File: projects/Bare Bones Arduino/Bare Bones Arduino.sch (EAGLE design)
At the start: 14 parts, among them IC1 AVR-MEGA8-P, J1 POWER_JACKPTH_LOCK

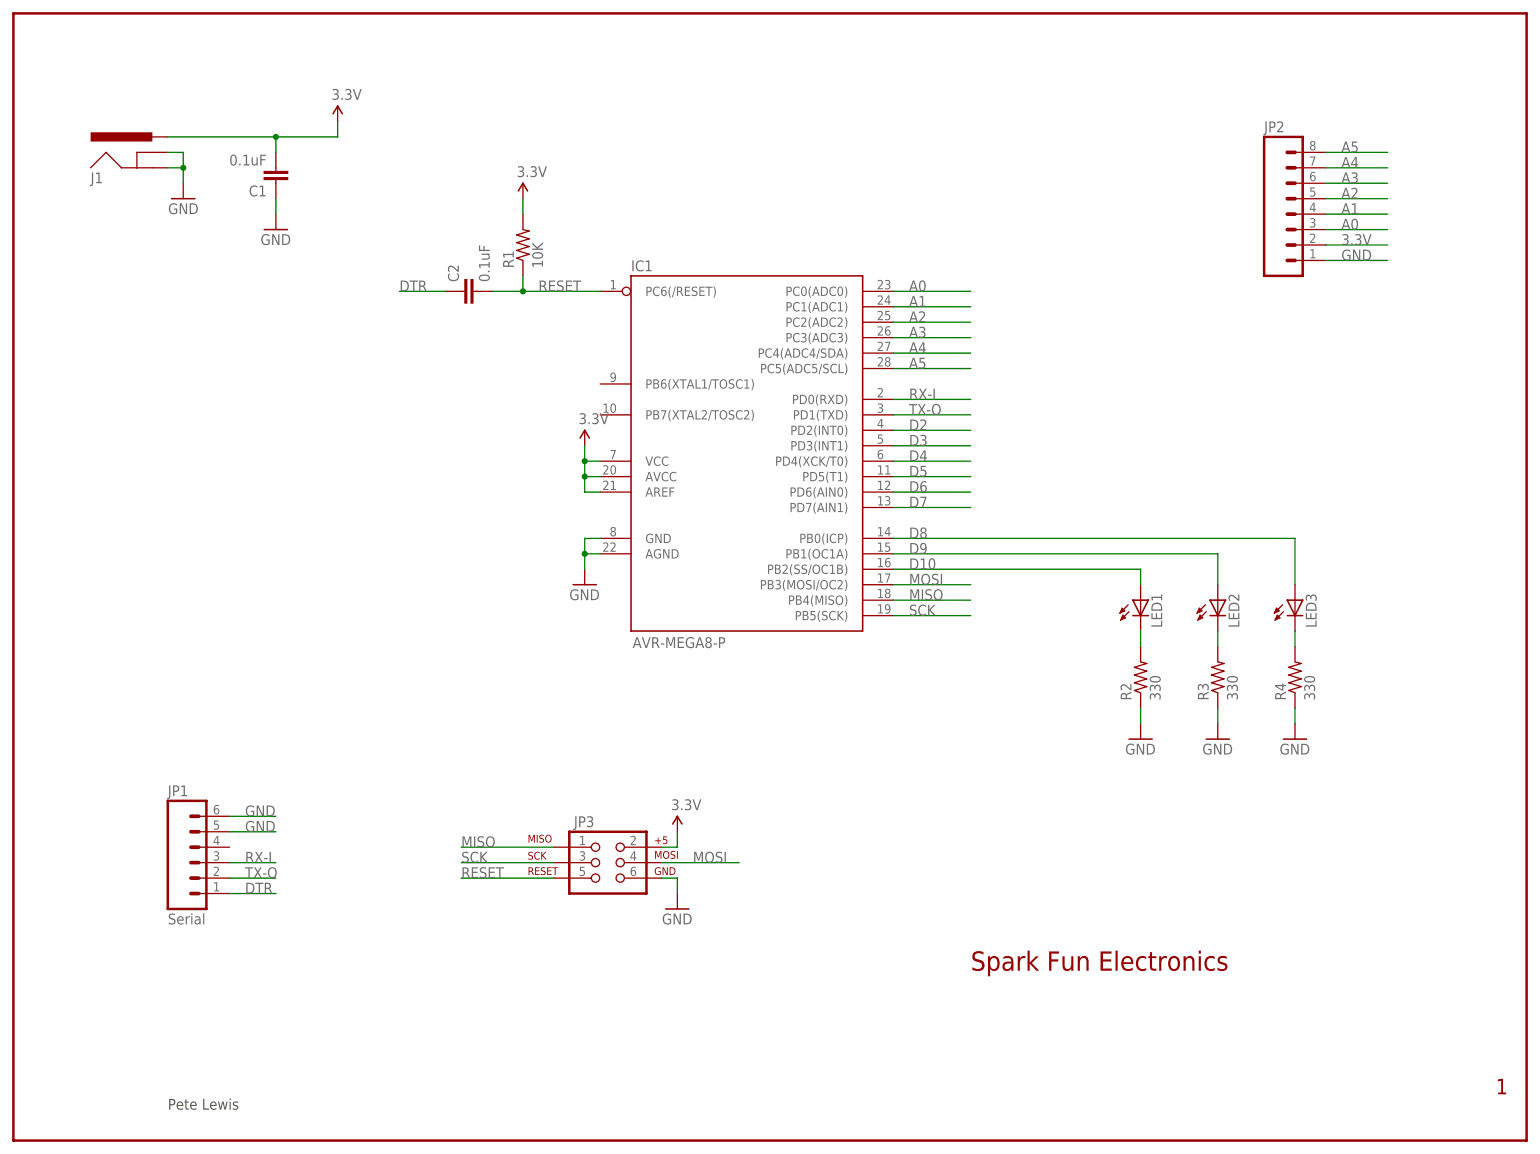
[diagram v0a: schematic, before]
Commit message: Updating Eagle files, adding documentation
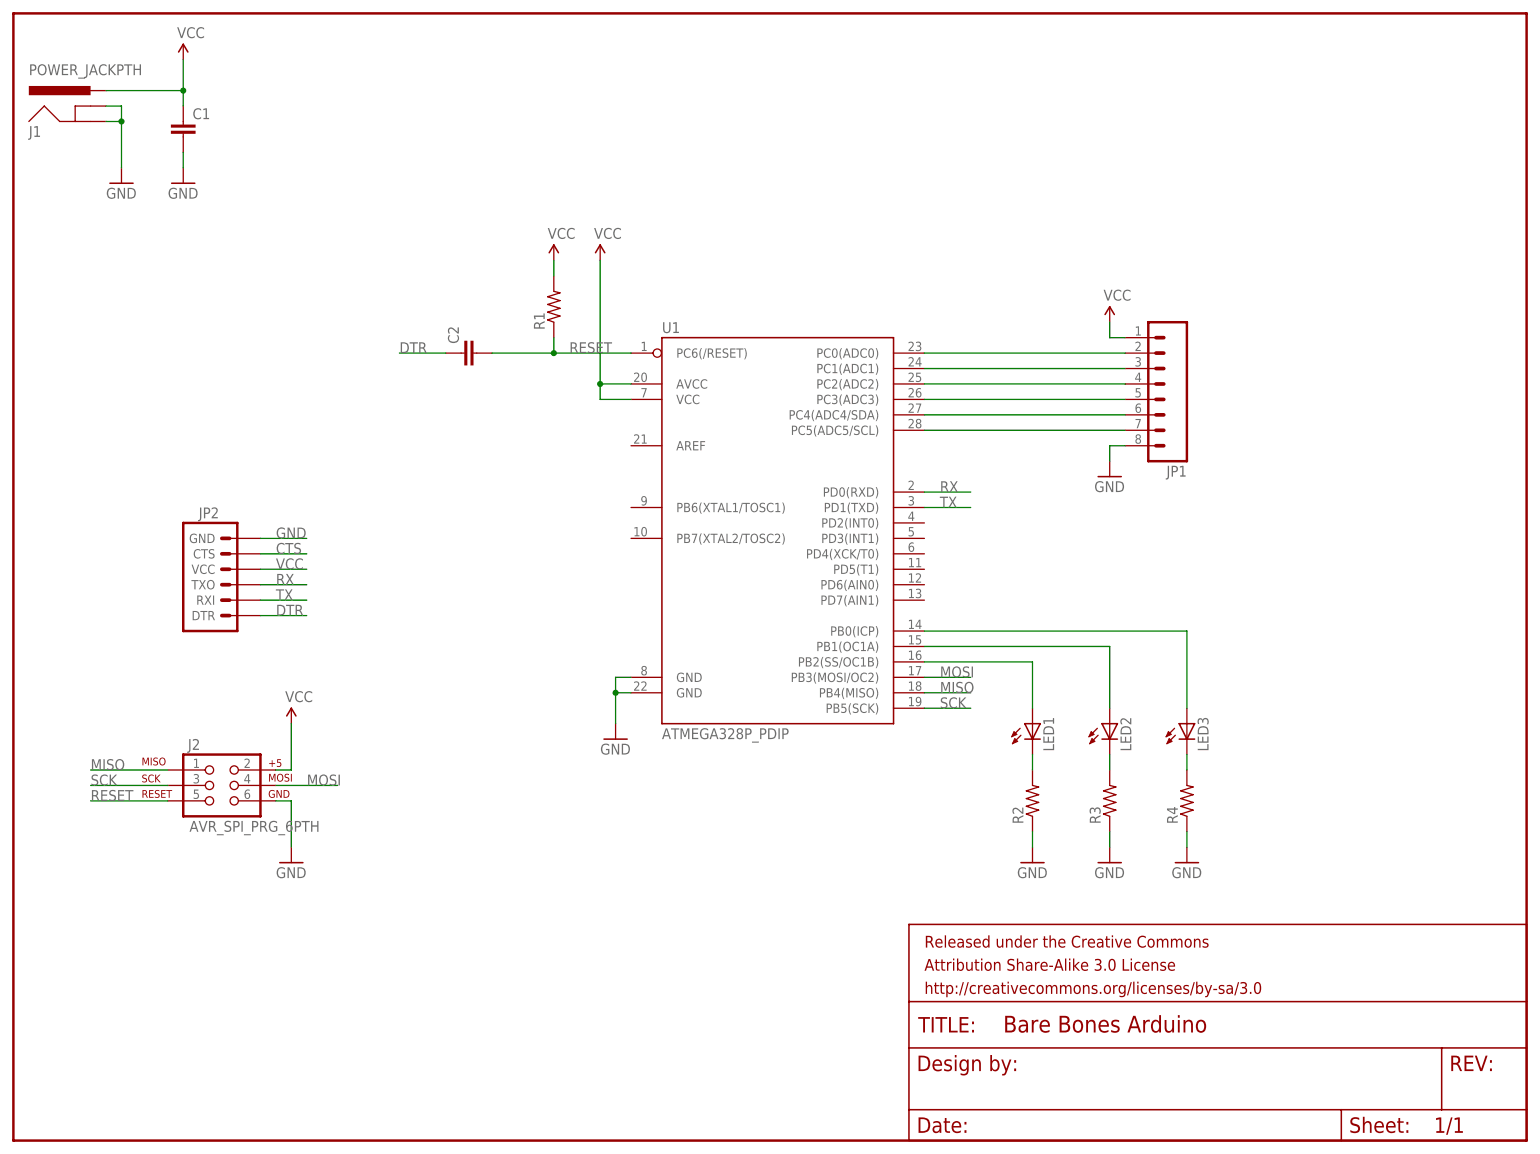
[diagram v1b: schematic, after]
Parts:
- removed IC1: AVR-MEGA8-P, Testing:AVR-MEGA8-PSIM
- removed JP3: AVR_SPI_PRG_6PTH, SparkFun:AVR_SPI_PRG_6PTH
- added FRAME1: FRAME-LETTER, SparkFun-Aesthetics:FRAME-LETTER
- added J2: AVR_SPI_PRG_6PTH, SparkFun-Connectors:AVR_SPI_PRG_6PTH
- added U1: ATMEGA328P_PDIP, SparkFun-DigitalIC:ATMEGA328P_PDIP
- C1, C2: value 0.1uF -> (none); device SparkFun:CAPCAP-PTH-SMALL-KIT -> SparkFun-Capacitors:CAPPTH
- J1: value POWER_JACKPTH_LOCK -> POWER_JACKPTH; device SparkFun:POWER_JACKPTH_LOCK -> SparkFun-Connectors:POWER_JACKPTH
- JP1: value Serial -> (none); device unclepetes:M06-SFENOSILK -> SparkFun-Connectors:M081X08
- JP2: device unclepetes:M08NOSILK -> SparkFun-Connectors:ARDUINO_SERIAL_PROGRAMPTH
- LED1, LED2, LED3: device SparkFun:LED5MM -> SparkFun-LED:LED5MM
- R1: value 10K -> (none); device SparkFun:RESISTORAXIAL-0.3-KIT -> SparkFun-Resistors:RESISTORPTH-1/4W
- R2, R3, R4: value 330 -> (none); device SparkFun:RESISTORAXIAL-0.3-KIT -> SparkFun-Resistors:RESISTORPTH-1/4W
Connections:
- removed net 3.3V: C1.2, IC1.AREF, IC1.AVCC, IC1.VCC@1, J1.PWR, JP2.2, JP3.2, R1.2
- removed net A0: IC1.PC0(ADC0), JP2.3
- removed net A1: IC1.PC1(ADC1), JP2.4
- removed net A2: IC1.PC2(ADC2), JP2.5
- removed net A3: IC1.PC3(ADC3), JP2.6
- removed net A4: IC1.PC4(ADC4/SDA), JP2.7
- removed net A5: IC1.PC5(ADC5/SCL), JP2.8
- removed net D10: IC1.PB2(SS/OC1B), LED1.A
- removed net D2: IC1.PD2(INT0)
- removed net D3: IC1.PD3(INT1)
- removed net D4: IC1.PD4(XCK/T0)
- removed net D5: IC1.PD5(T1)
- removed net D6: IC1.PD6(AIN0)
- removed net D7: IC1.PD7(AIN1)
- removed net D8: IC1.PB0(ICP), LED3.A
- removed net D9: IC1.PB1(OC1A), LED2.A
- removed net RX-I: IC1.PD0(RXD), JP1.3
- removed net TX-O: IC1.PD1(TXD), JP1.2
- new net CTS: JP2.CTS
- new net N$1: LED1.A, U1.PB2(SS/OC1B)
- new net N$10: JP1.5, U1.PC3(ADC3)
- new net N$11: JP1.6, U1.PC4(ADC4/SDA)
- new net N$12: JP1.7, U1.PC5(ADC5/SCL)
- new net N$2: LED2.A, U1.PB1(OC1A)
- new net N$3: LED3.A, U1.PB0(ICP)
- new net N$7: JP1.2, U1.PC0(ADC0)
- new net N$8: JP1.3, U1.PC1(ADC1)
- new net N$9: JP1.4, U1.PC2(ADC2)
- new net RX: JP2.TXO, U1.PD0(RXD)
- new net TX: JP2.RXI, U1.PD1(TXD)
- new net VCC: C1.1, J1.PWR, J2.2, JP1.1, JP2.VCC, R1.2, U1.AVCC, U1.VCC
- net DTR: now also JP2.DTR; no longer JP1.1
- net GND: now also C1.2, J2.6, JP1.8, JP2.GND, U1.GND@1, U1.GND@2; no longer C1.1, IC1.AGND, IC1.GND@1, JP1.5, JP1.6, JP2.1, JP3.6
- net MISO: now also J2.1, U1.PB4(MISO); no longer IC1.PB4(MISO), JP3.1
- net MOSI: now also J2.4, U1.PB3(MOSI/OC2); no longer IC1.PB3(MOSI/OC2), JP3.4
- net RESET: now also J2.5, U1.PC6(/RESET); no longer IC1.PC6(/RESET), JP3.5
- net SCK: now also J2.3, U1.PB5(SCK); no longer IC1.PB5(SCK), JP3.3
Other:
- note removed: "1"
- note removed: "Pete Lewis"
- note removed: "Spark Fun Electronics"
- moved on the sheet: C1, C2, J1, LED1, LED2, LED3, R1, R2, R3, R4
